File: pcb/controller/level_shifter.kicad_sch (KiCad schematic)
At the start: 3 parts

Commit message: cleaned up
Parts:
- renumbered Q to Q?, R to R?
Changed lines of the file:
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@@
 	(paper "A4")
+	(junction
+		(at 91.44 62.23)
+		(diameter 0)
+		(color 0 0 0 0)
+	)
 	(junction
 		(at 104.14 81.28)
@@
 	(wire
 		(pts
-			(xy 104.14 62.23) (xy 104.14 68.58)
+			(xy 91.44 60.96) (xy 91.44 62.23)
+		)
+		(stroke
+			(width 0)
+			(type default)
+		)
+	)
+	(wire
+		(pts
+			(xy 104.14 60.96) (xy 104.14 68.58)
 		)
 		(stroke
@@
 	(wire
 		(pts
-			(xy 86.36 62.23) (xy 96.52 62.23)
+			(xy 86.36 62.23) (xy 91.44 62.23)
 		)
 		(stroke
@@
 		(pts
 			(xy 96.52 62.23) (xy 96.52 73.66)
+		)
+		(stroke
+			(width 0)
+			(type default)
+		)
+	)
+	(wire
+		(pts
+			(xy 91.44 62.23) (xy 96.52 62.23)
 		)
 		(stroke
@@
 	(hierarchical_label "LV"
 		(shape input)
-		(at 91.44 62.23 90)
+		(at 91.44 60.96 90)
 		(effects
 			(font
@@
 	(hierarchical_label "HV"
 		(shape input)
-		(at 104.14 62.23 90)
+		(at 104.14 60.96 90)
 		(effects
 			(font
@@
 		(dnp no)
 		(fields_autoplaced yes)
-		(property "Reference" "Q"
+		(property "Reference" "Q?"
 			(at 96.52 85.09 90)
 			(effects
@@
 		(instances
 			(project "controller"
+				(path "/c599d8cf-7937-49be-b4ed-eac09167ead4/688f6757-198f-4f2c-ba04-8707221b0c5d/4aebe67b-79fa-4b22-b72a-a1db0ca6fc19"
+					(reference "Q?")
+					(unit 1)
+				)
 				(path "/c599d8cf-7937-49be-b4ed-eac09167ead4/688f6757-198f-4f2c-ba04-8707221b0c5d/7f988a32-c57f-4597-b4af-167af38a415b"
 					(reference "Q2")
@@
 		(dnp no)
 		(fields_autoplaced yes)
-		(property "Reference" "R"
+		(property "Reference" "R?"
 			(at 106.68 71.1199 0)
 			(effects
@@
 		(instances
 			(project "controller"
+				(path "/c599d8cf-7937-49be-b4ed-eac09167ead4/688f6757-198f-4f2c-ba04-8707221b0c5d/4aebe67b-79fa-4b22-b72a-a1db0ca6fc19"
+					(reference "R?")
+					(unit 1)
+				)
 				(path "/c599d8cf-7937-49be-b4ed-eac09167ead4/688f6757-198f-4f2c-ba04-8707221b0c5d/7f988a32-c57f-4597-b4af-167af38a415b"
 					(reference "R4")

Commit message: impl eFuse
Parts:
- gave numbers to parts that had none: 2
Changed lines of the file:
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@@
 		(dnp no)
 		(fields_autoplaced yes)
-		(property "Reference" "Q?"
+		(property "Reference" "Q1"
 			(at 96.52 85.09 90)
 			(effects
@@
 			(project "controller"
 				(path "/c599d8cf-7937-49be-b4ed-eac09167ead4/688f6757-198f-4f2c-ba04-8707221b0c5d/4aebe67b-79fa-4b22-b72a-a1db0ca6fc19"
-					(reference "Q?")
+					(reference "Q1")
 					(unit 1)
 				)
@@
 		(dnp no)
 		(fields_autoplaced yes)
-		(property "Reference" "R?"
+		(property "Reference" "R22"
 			(at 106.68 71.1199 0)
 			(effects
@@
 			(project "controller"
 				(path "/c599d8cf-7937-49be-b4ed-eac09167ead4/688f6757-198f-4f2c-ba04-8707221b0c5d/4aebe67b-79fa-4b22-b72a-a1db0ca6fc19"
-					(reference "R?")
-					(unit 1)
-				)
+					(reference "R22")
+					(unit 1)
+				)

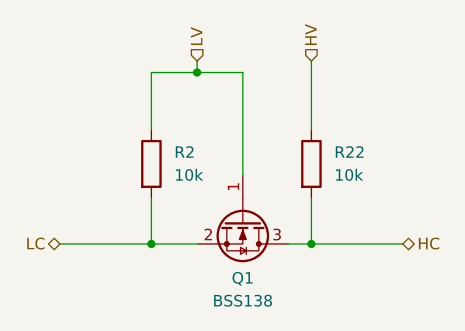
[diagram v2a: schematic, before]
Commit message: added lcsc numbers to all components and added ESD protection
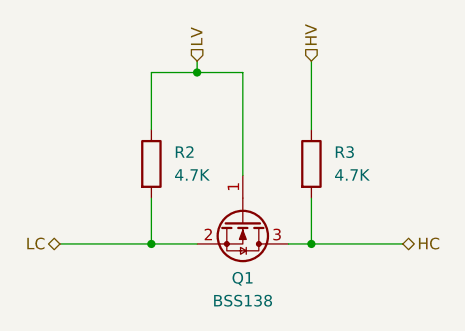
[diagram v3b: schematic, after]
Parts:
- removed R22: 10k, Resistor_SMD:R_1206_3216Metric, symbol Device:R
- added R3: 4.7K, Resistor_SMD:R_1206_3216Metric, symbol Device:R
- Q1: LCSC (none) -> C40912
- R2: value 10k -> 4.7K; LCSC (none) -> C2907499
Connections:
- net HC: now also R3.2
- net HV: now also R3.1
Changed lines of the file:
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@@
+			)
+		)
+		(property "LCSC" "C40912"
+			(at 96.52 78.74 90)
+			(effects
+				(font
+					(size 1.27 1.27)
+				)
+				(hide yes)
 			)
 		)
@@
 					(unit 1)
 				)
-				(path "/c599d8cf-7937-49be-b4ed-eac09167ead4/688f6757-198f-4f2c-ba04-8707221b0c5d/7f988a32-c57f-4597-b4af-167af38a415b"
+				(path "/c599d8cf-7937-49be-b4ed-eac09167ead4/688f6757-198f-4f2c-ba04-8707221b0c5d/b848546a-4430-427d-8a16-bcd4f77a363d"
 					(reference "Q2")
 					(unit 1)
@@
 			)
 		)
-		(property "Value" "10k"
+		(property "Value" "4.7K"
 			(at 88.9 73.6599 0)
 			(effects
@@
 			)
 		)
-		(pin "2"
+		(property "LCSC" "C2907499"
+			(at 86.36 72.39 90)
+			(effects
+				(font
+					(size 1.27 1.27)
+				)
+				(hide yes)
+			)
 		)
 		(pin "1"
+		)
+		(pin "2"
 		)
 		(instances
@@
 					(unit 1)
 				)
-				(path "/c599d8cf-7937-49be-b4ed-eac09167ead4/688f6757-198f-4f2c-ba04-8707221b0c5d/7f988a32-c57f-4597-b4af-167af38a415b"
-					(reference "R3")
+				(path "/c599d8cf-7937-49be-b4ed-eac09167ead4/688f6757-198f-4f2c-ba04-8707221b0c5d/b848546a-4430-427d-8a16-bcd4f77a363d"
+					(reference "R4")
 					(unit 1)
 				)
@@
 		(dnp no)
 		(fields_autoplaced yes)
-		(property "Reference" "R22"
+		(property "Reference" "R3"
 			(at 106.68 71.1199 0)
 			(effects
@@
 			)
 		)
-		(property "Value" "10k"
+		(property "Value" "4.7K"
 			(at 106.68 73.6599 0)
 			(effects
@@
 			)
 		)
-		(pin "2"
+		(property "LCSC" "C2907499"
+			(at 104.14 72.39 90)
+			(effects
+				(font
+					(size 1.27 1.27)
+				)
+				(hide yes)
+			)
 		)
 		(pin "1"
+		)
+		(pin "2"
 		)
 		(instances
 			(project "controller"
 				(path "/c599d8cf-7937-49be-b4ed-eac09167ead4/688f6757-198f-4f2c-ba04-8707221b0c5d/4aebe67b-79fa-4b22-b72a-a1db0ca6fc19"
+					(reference "R3")
+					(unit 1)
+				)
+				(path "/c599d8cf-7937-49be-b4ed-eac09167ead4/688f6757-198f-4f2c-ba04-8707221b0c5d/b848546a-4430-427d-8a16-bcd4f77a363d"
 					(reference "R22")
 					(unit 1)
 				)
-				(path "/c599d8cf-7937-49be-b4ed-eac09167ead4/688f6757-198f-4f2c-ba04-8707221b0c5d/7f988a32-c57f-4597-b4af-167af38a415b"
-					(reference "R4")
-					(unit 1)
-				)
